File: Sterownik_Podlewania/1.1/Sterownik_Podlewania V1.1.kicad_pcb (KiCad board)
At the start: 2 copper layers, 175 x 115 mm, 74 parts, among them J1 RJ45, J10 Screw_Terminal_01x02, J11 Screw_Terminal_01x02, J12 Barrel_Jack_MountingPin, J2 RJ45, J3 Conn_01x04_Socket, J4 RJ45, J5 Screw_Terminal_01x02, J6 Screw_Terminal_01x02, J7 Screw_Terminal_01x02, J8 Screw_Terminal_01x02, J9 Screw_Terminal_01x02, SW1 SW_Nidec_CAS-120A1, SW2 SW_Nidec_CAS-120A1, SW3 SW_Push_Dual_x2, SW4 SW_Push_Dual_x2, SW5 SW_Push_Dual_x2, SW6 SW_Push_Dual_x2, U1 ESP32-DEVKITC, U10 LD1117S33TR_SOT223, U3 757, U4 757, U5 HHG1D-1, U6 HHG1D-1, U7 HHG1D-1, U8 HHG1D-1, U9 HHG1D-1

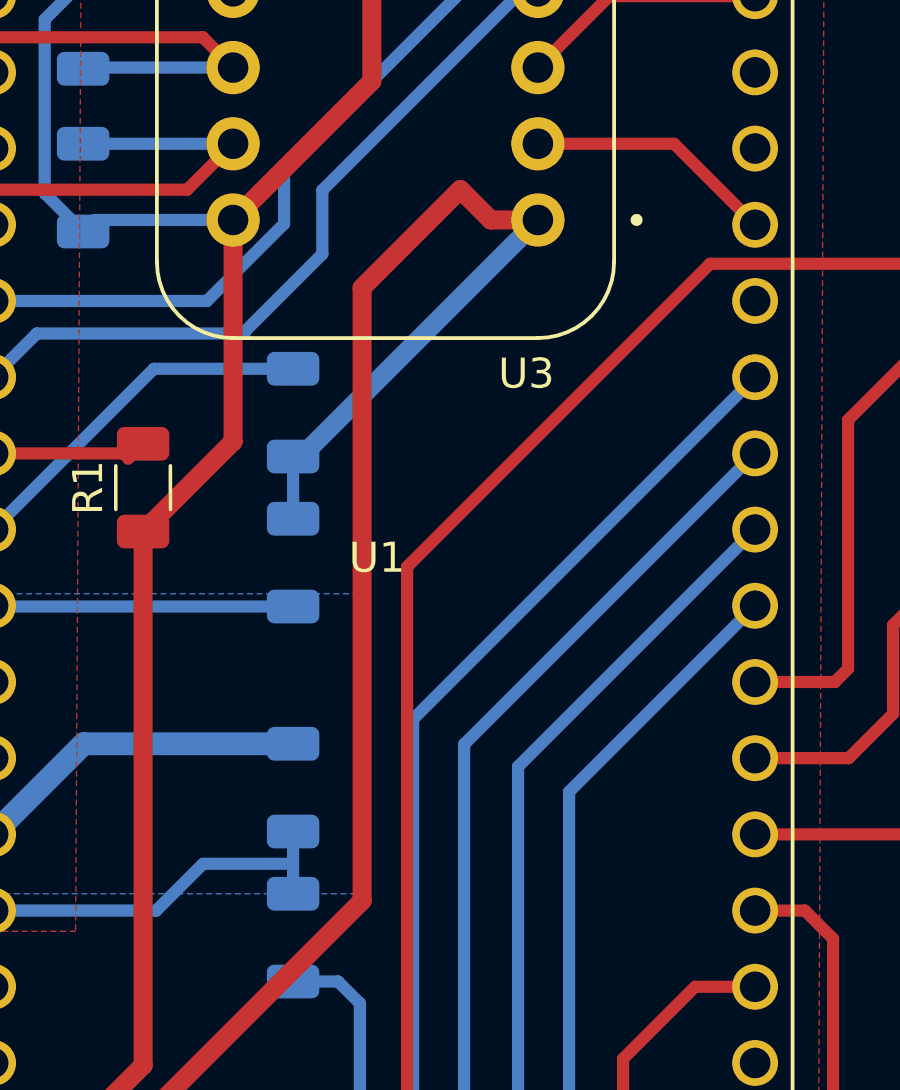
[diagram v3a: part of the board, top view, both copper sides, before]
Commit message: Poprawki moduł zasilania, stowrzenie płytki, zostało trochę błędów, zapomniałem dać mouting holes
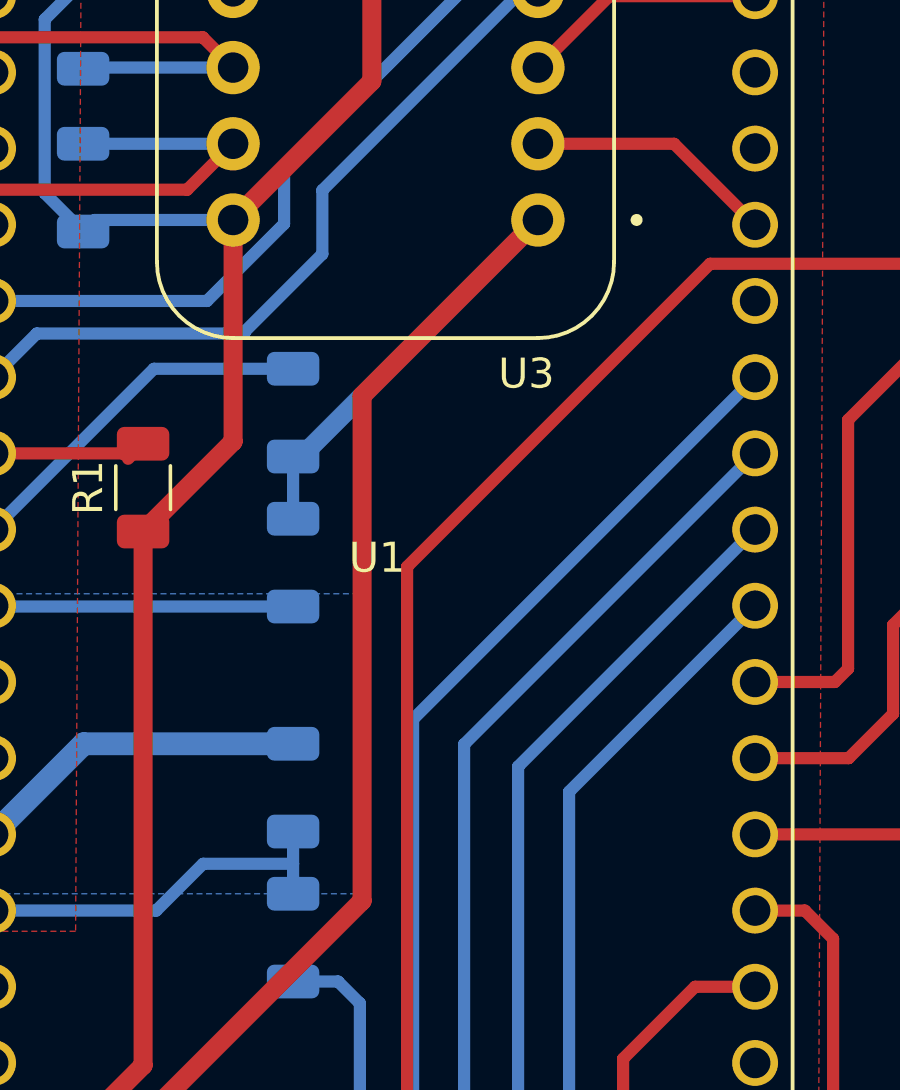
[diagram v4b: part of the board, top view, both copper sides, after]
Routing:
- net +3.3V: track 378.8 -> 375.9 mm
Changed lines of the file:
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@@
-	)
-	(segment
-		(start 187.3 102.735144)
-		(end 187.3 82.3)
-		(width 0.635)
-		(layer "F.Cu")
-		(net 7)
 	)
 	(segment
@@
 		(start 154.15 121.15)
 		(end 154.15 132.6)
-		(width 0.635)
-		(layer "F.Cu")
-		(net 7)
-	)
-	(segment
-		(start 187.3 82.3)
-		(end 190.575 79.025)
 		(width 0.635)
 		(layer "F.Cu")
@@
 		(start 192.7 58.2)
 		(end 191.075 58.2)
-		(width 0.635)
-		(layer "F.Cu")
-		(net 7)
-	)
-	(segment
-		(start 190.575 79.025)
-		(end 191.59 80.04)
-		(width 0.635)
-		(layer "F.Cu")
-		(net 7)
-	)
-	(segment
-		(start 154.15 121.15)
-		(end 168.885144 121.15)
 		(width 0.635)
 		(layer "F.Cu")
@@
 	)
 	(segment
+		(start 154.15 121.15)
+		(end 168.885144 121.15)
+		(width 0.635)
+		(layer "F.Cu")
+		(net 7)
+	)
+	(segment
 		(start 191.075 57.475)
 		(end 192.025 56.525)
+		(width 0.635)
+		(layer "F.Cu")
+		(net 7)
+	)
+	(segment
+		(start 168.885144 121.15)
+		(end 187.3 102.735144)
 		(width 0.635)
 		(layer "F.Cu")
@@
 		(end 58.9458 122.7408)
 		(width 0.4064)
+		(layer "F.Cu")
+		(net 7)
+	)
+	(segment
+		(start 187.3 85.9)
+		(end 193.16 80.04)
+		(width 0.635)
 		(layer "F.Cu")
 		(net 7)
@@
 	)
 	(segment
-		(start 168.885144 121.15)
-		(end 187.3 102.735144)
-		(width 0.635)
-		(layer "F.Cu")
-		(net 7)
-	)
-	(segment
-		(start 191.59 80.04)
-		(end 193.16 80.04)
-		(width 0.635)
-		(layer "F.Cu")
-		(net 7)
-	)
-	(segment
 		(start 58.9458 104.4833)
 		(end 58.9458 101.7117)
@@
 		(layer "F.Cu")
 		(net 7)
+	)
+	(segment
+		(start 187.3 102.735144)
+		(end 187.3 85.9)
+		(width 0.635)
+		(layer "F.Cu")
+		(net 7)

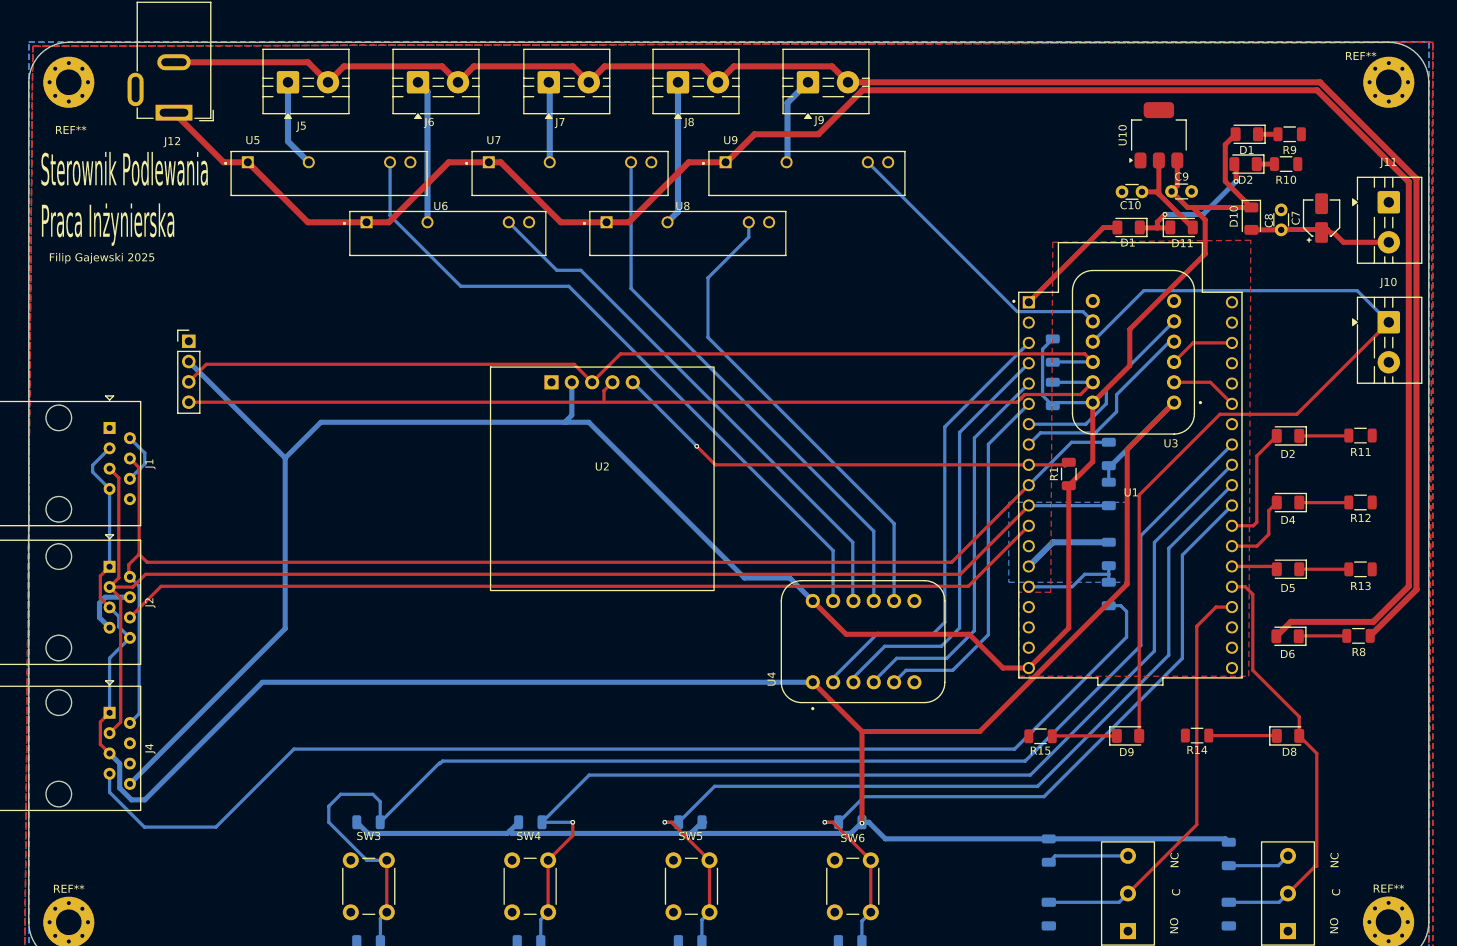
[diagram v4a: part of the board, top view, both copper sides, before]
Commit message: Werja plików podesłana Mariuszkowi, dodane opisy i numeracja poprawna dla steronwika, w module poprawniono opis złącze ethernet
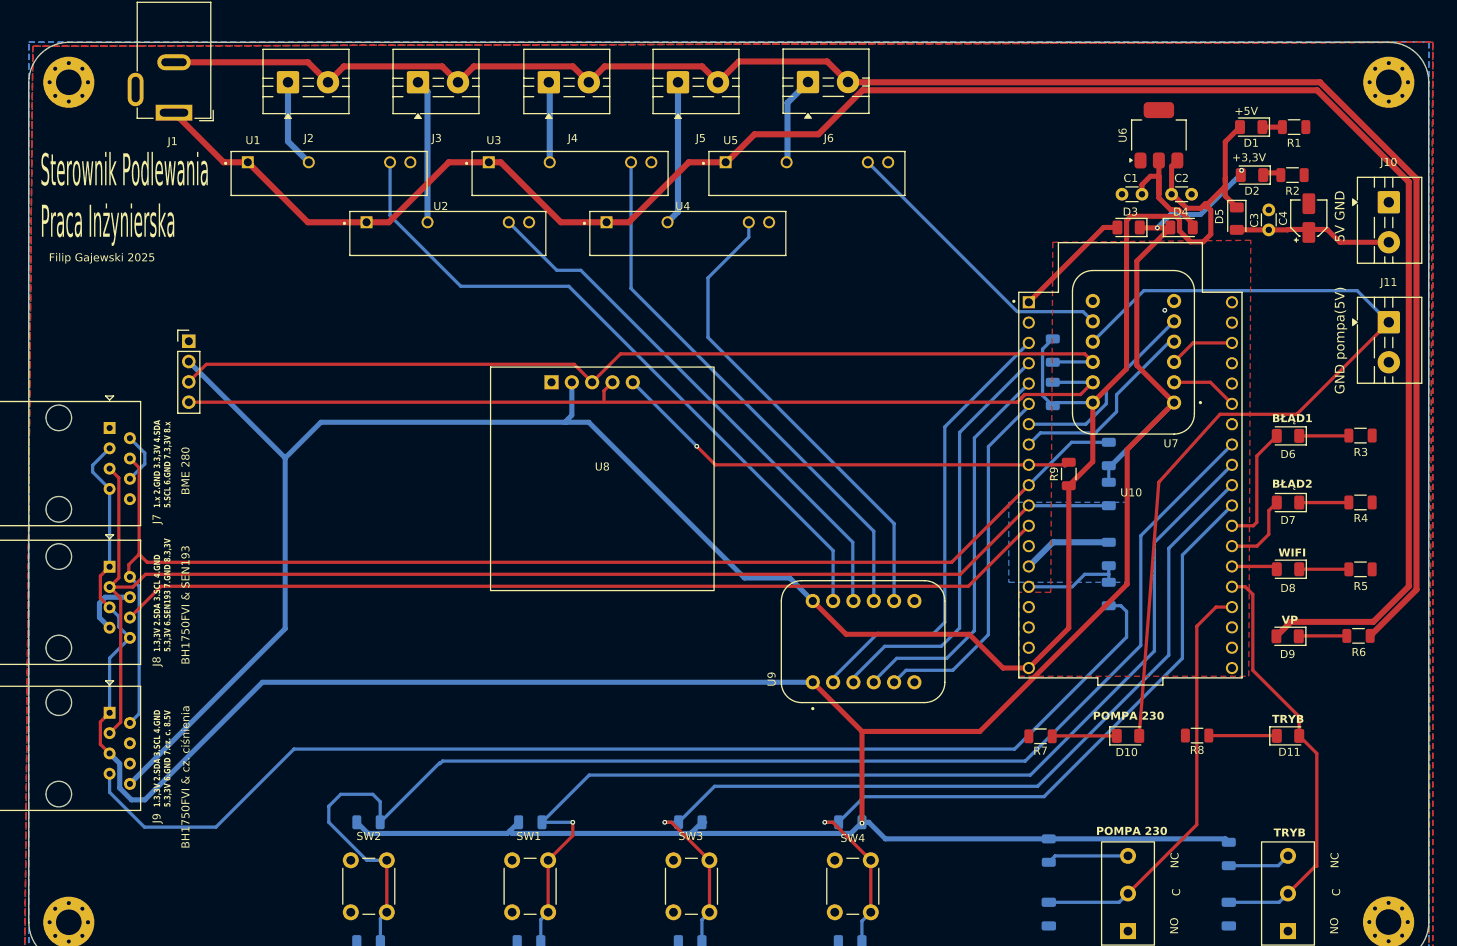
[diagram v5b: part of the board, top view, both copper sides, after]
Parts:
- moved D5 1.82 mm to (201.0, 57.0)
- moved C4 1.60 mm to (210.0, 57.0)
- moved D2 1.59 mm to (202.9, 51.6)
- moved R2 1.59 mm to (208.0, 51.6)
- moved C3 1.55 mm to (205.0, 58.5)
- moved D1 1.05 mm to (202.8, 45.6)
- moved R1 1.05 mm to (208.2, 45.6)
- moved C2 0.35 mm to (192.8, 54.0)
- moved C1 0.30 mm to (189.2, 54.0)
- renumbered C10 to C1, C3 to C10, C9 to C2, C8 to C3, C7 to C4, C1 to C5, C2 to C6, C6 to C7, C5 to C8, C4 to C9, D9 to D10, D8 to D11, D1 to D3, D11 to D4, D10 to D5, D2 to D6, D4 to D7, D5 to D8, D6 to D9, J12 to J1, J11 to J10, J10 to J11, J3 to J12, J5 to J2, J6 to J3, J7 to J4, J8 to J5, J9 to J6, J1 to J7, J2 to J8, J4 to J9, R9 to R1, R6 to R10, R7 to R11, R4 to R12, R5 to R13, R3 to R14, R2 to R15, R21 to R18, R20 to R19, R10 to R2, R19 to R20, R18 to R21, R11 to R3, R12 to R4, R13 to R5, R8 to R6, R15 to R7, R14 to R8, R1 to R9, SW4 to SW1, SW3 to SW2, SW5 to SW3, SW6 to SW4, SW2 to SW5, SW1 to SW6, U5 to U1, U1 to U10, U6 to U2, U7 to U3, U8 to U4, U9 to U5, U10 to U6, U3 to U7, U2 to U8, U4 to U9
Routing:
- net +3.3V: track 375.9 -> 400.1 mm
- net +5V: track 287.0 -> 297.3 mm
- net Net-(D4-A): track 12.4 -> 16.7 mm
- net Net-(D5-A): track 17.9 -> 19.7 mm
- net /Pompa_230_5V: track 111.5 -> 110.4 mm
- net GND_VP: track 227.5 -> 228.0 mm
- net GND: vias 0 -> 1
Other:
- board text added: "+3,3V"
- board text added: "+5V"
- board text added: "1.3,3V 2.SDA 3.SCL 4.GND 5.3,3V 6.GND 7.cz. c. 8.5V"
- board text added: "1.3,3V 2.SDA 3.SCL 4.GND 5.3,3V 6.SEN193 7.GND 8.3,3V"
- board text added: "1.x 2.GND 3.3,3V 4.SDA 5.SCL 6.GND 7.3,3V 8.x"
- board text added: "5V GND"
- board text added: "BH1750FVI & SEN193"
- board text added: "BH1750FVI & cz. ciśnienia"
- board text added: "BME 280"
- board text added: "BŁĄD1"
- board text added: "BŁĄD2"
- board text added: "GND pompa(5V)"
- board text added: "POMPA 230"
- board text added: "TRYB"
- board text added: "VP"
- board text added: "WIFI"

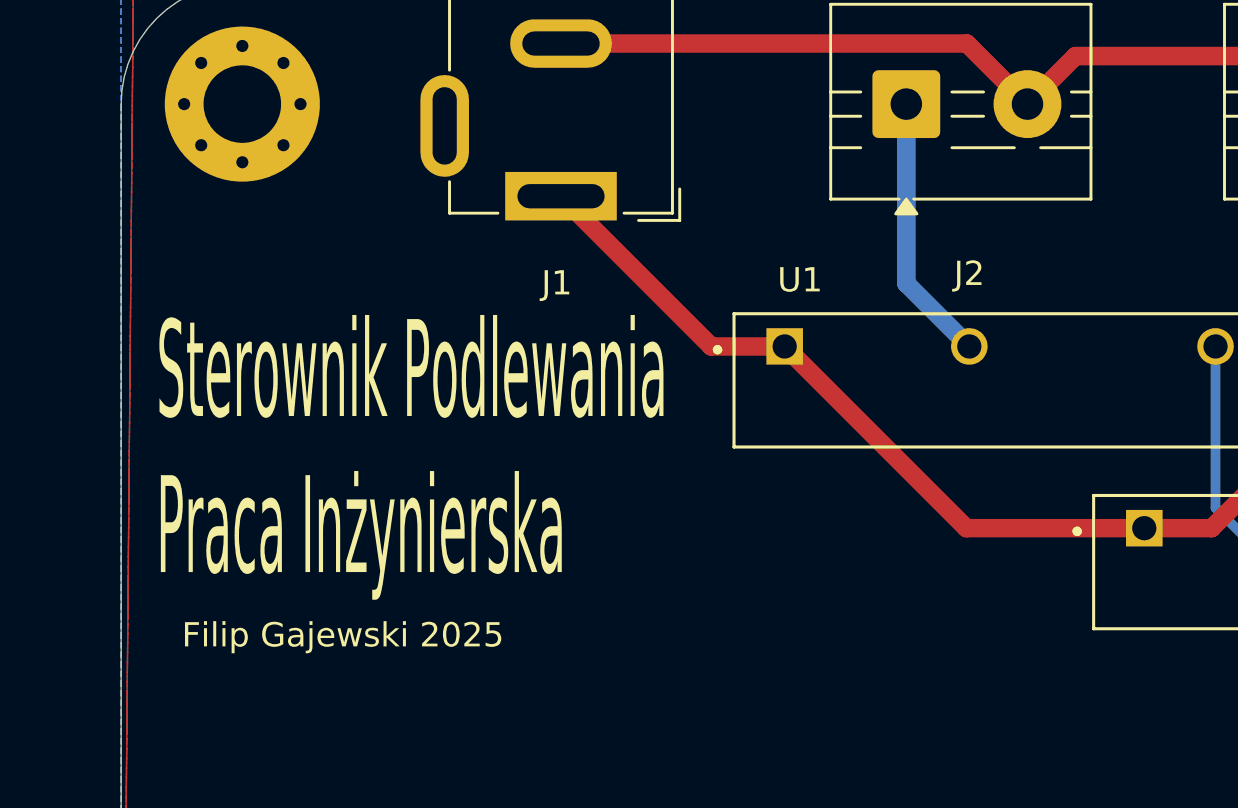
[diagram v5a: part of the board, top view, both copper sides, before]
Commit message: Kod websocket, kod stonka demo, kod sterownika - wszystkie taski poza bt wstepnie ogarniete
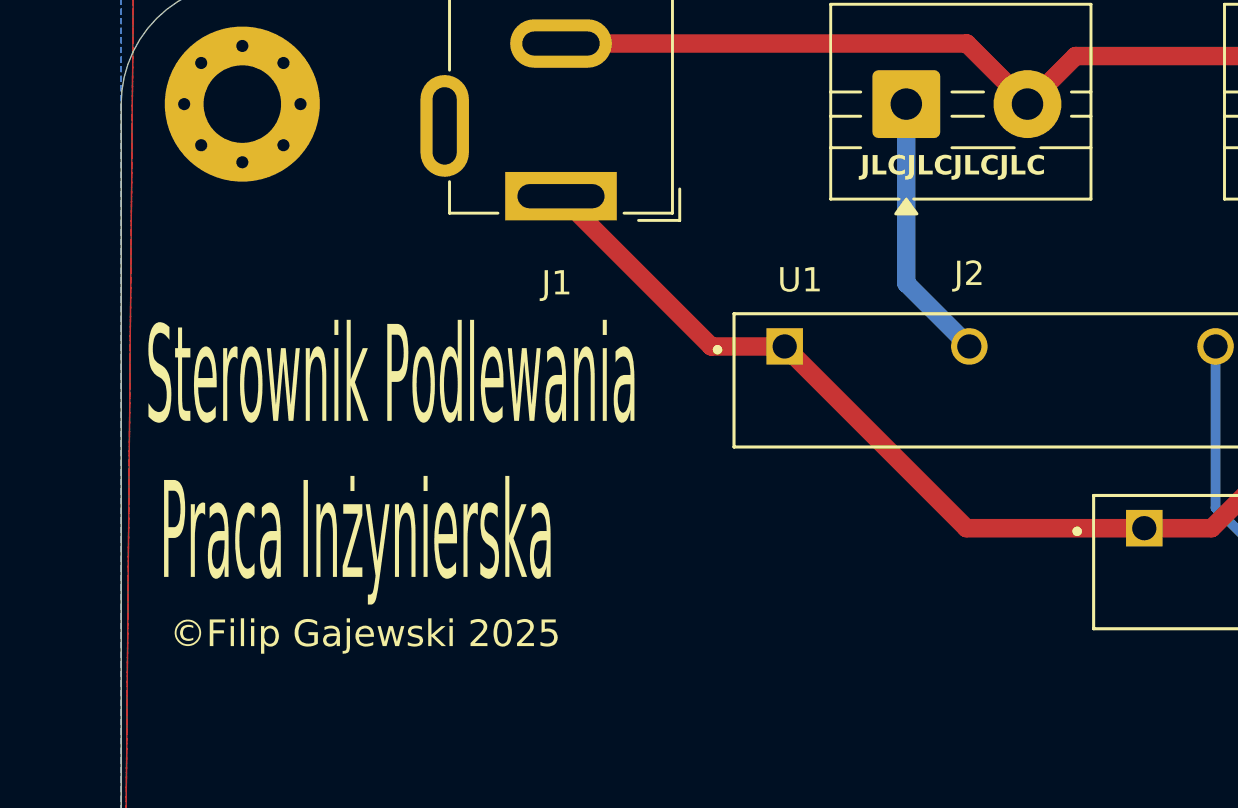
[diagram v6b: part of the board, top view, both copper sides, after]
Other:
- board text added: "JLCJLCJLCJLC"
- board text added: "©Filip Gajewski 2025"
- board text removed: "Filip Gajewski 2025"
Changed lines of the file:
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@@
 			(outputformat 1)
 			(mirror no)
-			(drillshape 1)
+			(drillshape 0)
 			(scaleselection 1)
-			(outputdirectory "")
+			(outputdirectory "F:/Pulpit/AIR/7_semestr/praca inzynierska/Gerberki/")
 		)
 	)
@@
 		)
 	)
+	(gr_text "JLCJLCJLCJLC"
+		(at 80.5 43 0)
+		(layer "F.SilkS")
+		(effects
+			(font
+				(size 0.8 0.8)
+				(thickness 0.2)
+				(bold yes)
+			)
+			(justify left bottom)
+		)
+	)
 	(gr_text "BŁĄD2\n"
 		(at 205.4 90.8 0)
@@
 		)
 	)
-	(gr_text "Filip Gajewski 2025\n"
-		(at 52.5 62.5 0)
+	(gr_text "©Filip Gajewski 2025\n"
+		(at 52 62.5 0)
 		(layer "F.SilkS")
 		(effects
 			(font
-				(size 1 1)
+				(size 1.1 1.1)
 				(thickness 0.15)
 			)
@@
 		)
 	)
-	(gr_text "Sterownik Podlewania\nPraca Inżynierska"
-		(at 51.45 59.8 0)
+	(gr_text "Sterownik Podlewania\n Praca Inżynierska"
+		(at 51 60 0)
 		(layer "F.SilkS")
 		(effects
 			(font
-				(size 4 1.4)
+				(size 4 1.35)
 				(thickness 0.15)
 			)
